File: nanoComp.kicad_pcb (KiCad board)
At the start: 2 copper layers, 90 x 70 mm, 22 parts, among them J1 USB_C_Receptacle_PowerOnly_6P, J2 USB_A, J3 USB_A, J4 Conn_01x06_Pin, J5 Conn_01x14, J6 Conn_01x04, SW1 SW_Wuerth_450301014042

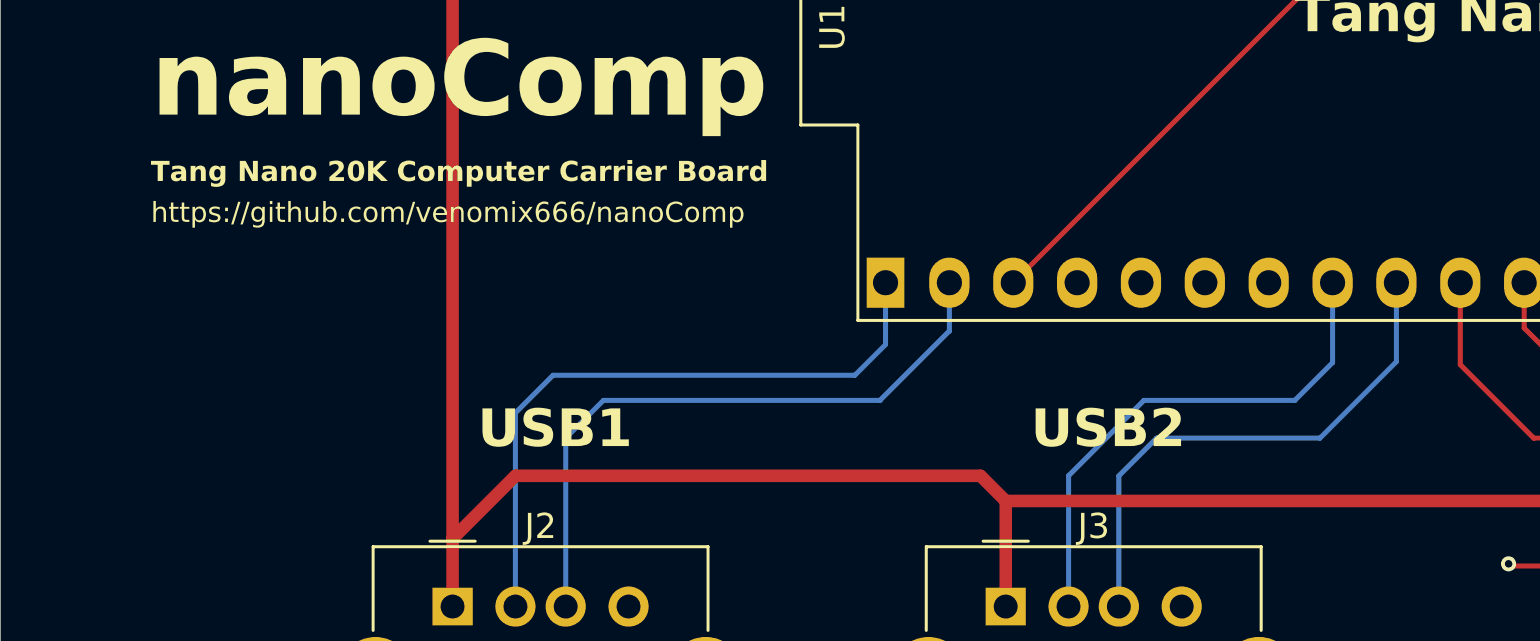
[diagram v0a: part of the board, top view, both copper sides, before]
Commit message: Added 15k pulldowns on USB data lines for master configuration
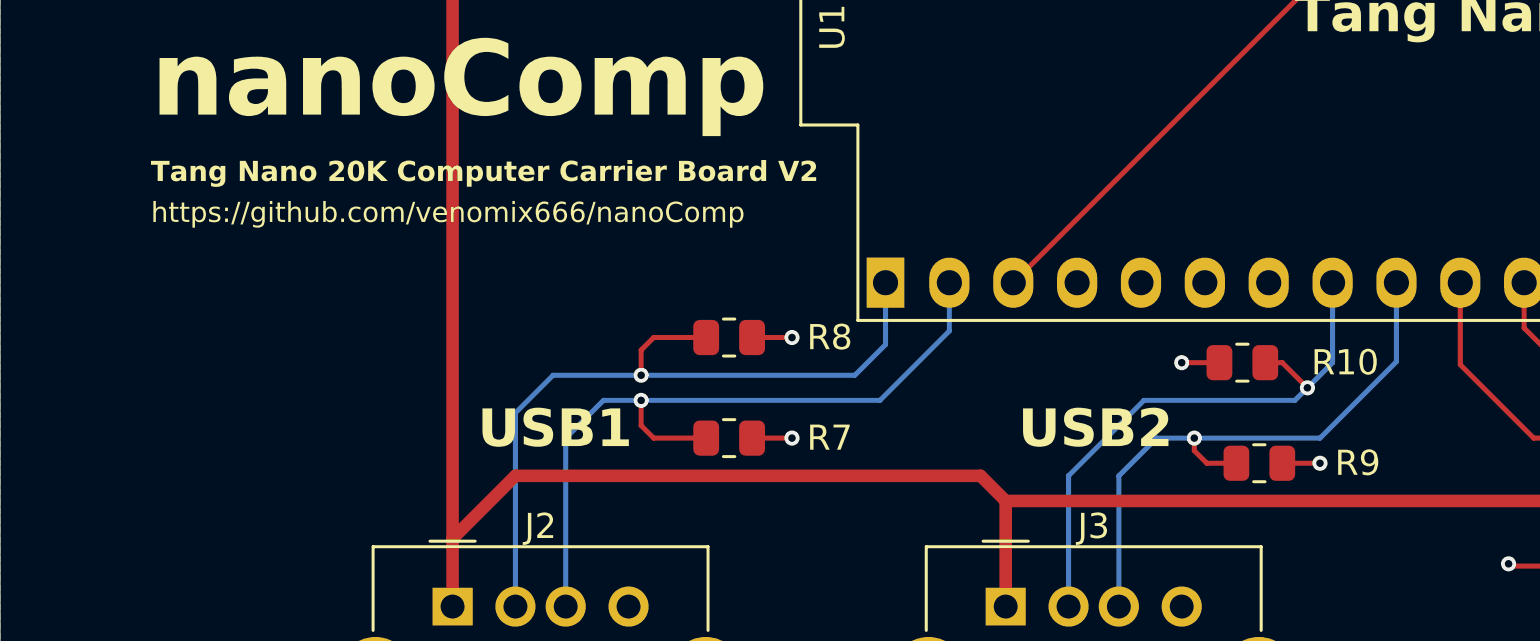
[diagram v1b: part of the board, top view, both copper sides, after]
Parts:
- added R10: 15k, Resistor_SMD:R_0805_2012Metric, F.Cu at (129.4, 110.0)
- added R7: 15k, Resistor_SMD:R_0805_2012Metric, F.Cu at (109.0, 113.0)
- added R8: 15k, Resistor_SMD:R_0805_2012Metric, F.Cu at (109.0, 109.0)
- added R9: 15k, Resistor_SMD:R_0805_2012Metric, F.Cu at (130.1, 114.0)
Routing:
- net GND: track 18.2 -> 24.4 mm, vias 6 -> 10
- net /USB_A_D-: track 25.4 -> 29.2 mm, vias 0 -> 1
- net /USB_A_D+: track 25.1 -> 28.9 mm, vias 0 -> 1
- net /USB_B_D+: track 20.7 -> 23.1 mm, vias 0 -> 1
- net /USB_B_D-: track 20.2 -> 22.3 mm, vias 0 -> 1
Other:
- board text added: "Tang Nano 20K Computer Carrier Board V2"
- board text removed: "Tang Nano 20K Computer Carrier Board"
